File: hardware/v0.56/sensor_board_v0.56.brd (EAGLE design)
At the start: 50.8 x 50.8 mm, 63 parts, among them J3 USB-MICROB, U10 TSL2591, U11 915MHz, U3 OPA344, U4 SI7021, U5 ATMEGA328P-MU, U6 ADMP401, U7 PMS7003, U8 MCP1703CB, U9 BMP280, X1 16 MHz

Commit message: update
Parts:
- added R9: 100K, Adafruit Feather 32u4 Bluefruit LE:MICROBUILDER__0402MP
- moved U$7 0.28 mm to (35.2, 1.42)
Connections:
- new net A1: U5.24
- new net A2: U5.25
- new net A3: U5.26
- new net A6: U5.19
- new net A7: U5.22
- new net N$13: R9.2, U$7.1
- net D5: now also U$7.7
- net GND: now also C2.1, J2.1, U$7.11
- net PWR: now also J2.2
- net SCL: now also U$7.10
- net SDA: now also U$7.9
- net VCC: now also C2.2, R9.1, U$7.6

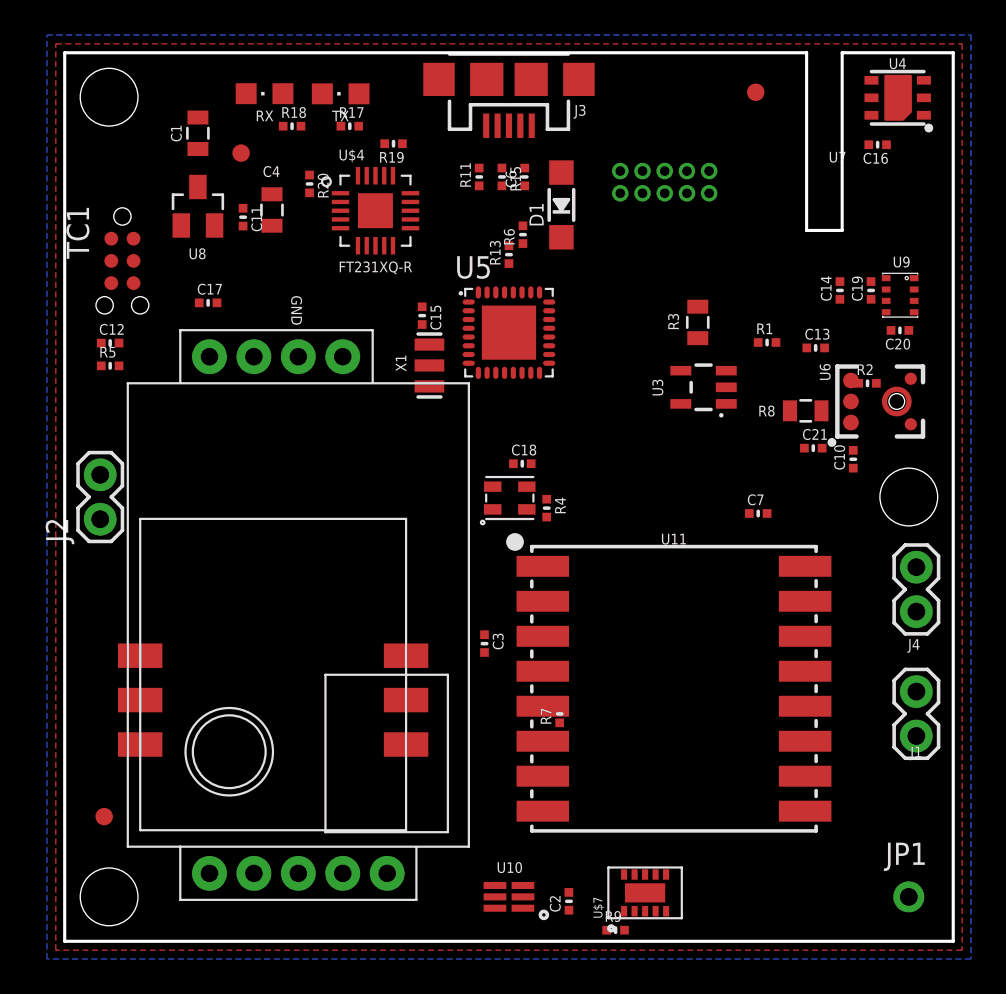
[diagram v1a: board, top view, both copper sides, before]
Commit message: Added Power Booster circuit; a lot of rearrangments
circuit traces still incomplete
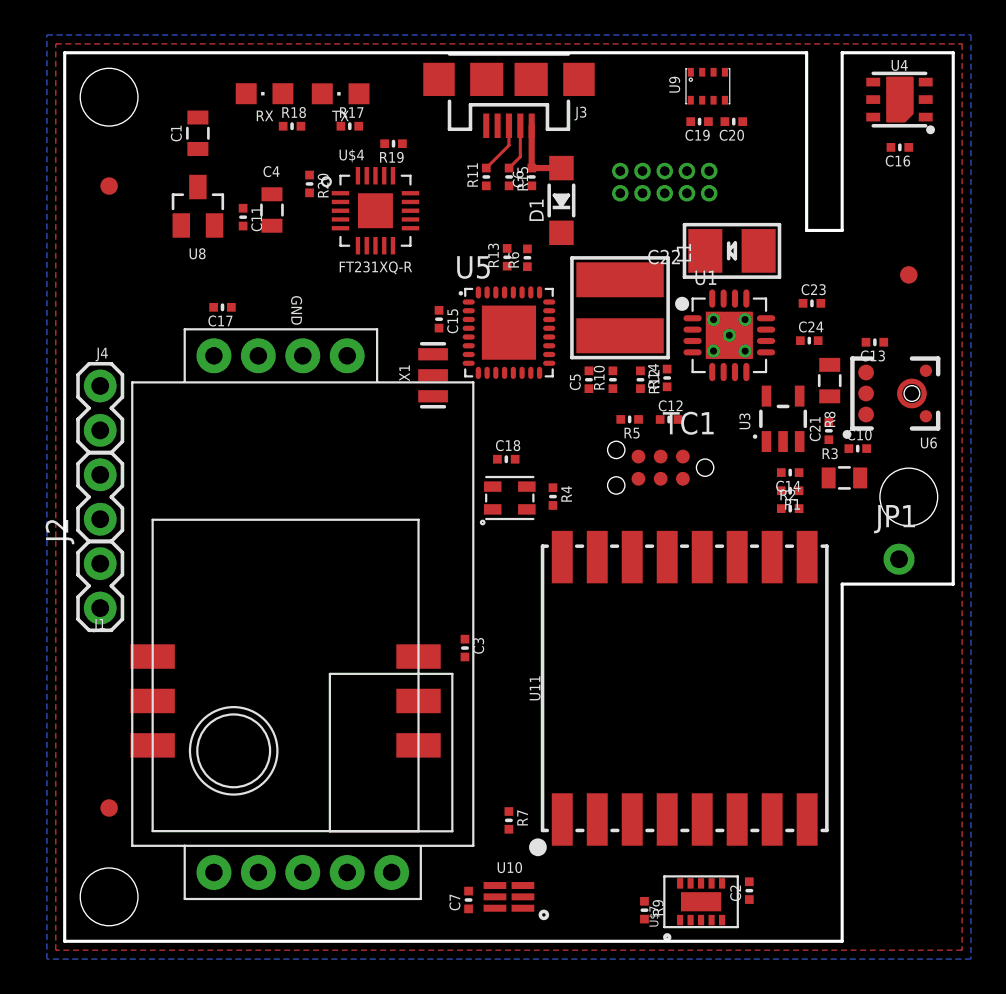
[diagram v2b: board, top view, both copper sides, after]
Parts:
- added C22: 100uF/6V, microbuilder:EIA3528-21/B-R
- added C23: 0.1uF, Adafruit Feather 32u4 Bluefruit LE:MICROBUILDER__0402MP
- added C24: 10uF, Adafruit Feather 32u4 Bluefruit LE:MICROBUILDER__0402MP
- added C5: 2.2uF, Adafruit Feather 32u4 Bluefruit LE:MICROBUILDER__0402MP
- added L1: VLC5045-6.8uH, microbuilder:INDUCTOR_5X5MM_TDK_VLC5045
- added R10: 1.87M, Adafruit Feather 32u4 Bluefruit LE:MICROBUILDER__0402MP
- added R12: 200K, Adafruit Feather 32u4 Bluefruit LE:MICROBUILDER__0402MP
- added R14: 340K, Adafruit Feather 32u4 Bluefruit LE:MICROBUILDER__0402MP
- added U1: TPS61090RSAR, microbuilder:PVQFN-16
- moved J4 47.3 mm to (2.03, 29.2), turned to 90 degrees
- moved J1 47.2 mm to (2.03, 19.1)
- moved TC1 33.0 mm to (34.1, 27.1), turned to 180 degrees
- moved C12 32.3 mm to (34.6, 29.8)
- moved R5 29.9 mm to (32.3, 29.8), turned to 180 degrees
- moved C7 27.6 mm to (23.1, 2.36), turned to 90 degrees
- moved JP1 19.3 mm to (47.7, 21.8)
- moved U9 16.2 mm to (36.8, 48.9), turned to 180 degrees
- moved C20 15.3 mm to (38.3, 46.9)
- moved C19 13.8 mm to (36.3, 46.9), turned to 180 degrees
- moved U$3 13.6 mm to (48.3, 38.1)
- moved R3 12.2 mm to (44.6, 26.5), turned to 0 degrees
- moved C14 10.8 mm to (41.5, 26.8), turned to 180 degrees
- moved C2 10.3 mm to (39.1, 2.90)
- moved R1 8.58 mm to (41.5, 25.8), turned to 180 degrees
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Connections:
- new net 5.0V: C22.+, C5.2, R10.2, U1.1, U1.15, U1.16
- new net ENABLE: R14.1, U1.11
- new net N$12: R10.1, R12.2, U1.14
- new net N$6: L1.P$2, U1.3, U1.4
- new net VBAT: R14.2
- net GND: now also C22.-, C23.1, C24.1, C5.1, R12.1, U1.10, U1.13, U1.5, U1.6, U1.7, U1.P$18, U1.P$19, U1.P$20, U1.P$21, U1.P$22, U1.THERMAL
- net PWR: now also C23.2, C24.2, L1.P$1, U1.8
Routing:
- net VBUS: track 0.00 -> 4.12 mm
- net N$33: track 0.00 -> 2.95 mm
- net N$32: track 0.00 -> 2.68 mm
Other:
- outline, holes or cut-outs redrawn
- board text removed: "U7"

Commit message: Adjustments
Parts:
- removed J4: (no value), SparkFun-Connectors:1X02
- moved C23 35.9 mm to (6.81, 37.7), turned to 90 degrees
- moved C24 34.2 mm to (8.59, 37.7), turned to 90 degrees
- moved RX 31.3 mm to (39.9, 35.4), turned to 0 degrees
- moved R18 27.9 mm to (38.1, 34.4), turned to 180 degrees
- moved TX 25.7 mm to (39.9, 39.4), turned to 0 degrees
- moved C22 25.3 mm to (14.1, 47.4), turned to 0 degrees
- moved U1 25.0 mm to (13.9, 41.5), turned to 270 degrees
- moved L1 24.8 mm to (7.62, 42.1), turned to 90 degrees
- moved R17 23.3 mm to (38.1, 38.2)
- moved R20 23.0 mm to (36.0, 36.6)
- moved J1 21.6 mm to (2.03, 40.6)
- moved C5 20.3 mm to (14.4, 45.1), turned to 0 degrees
- moved R14 18.2 mm to (17.4, 38.6), turned to 270 degrees
- moved R12 17.7 mm to (17.4, 40.6), turned to 90 degrees
- moved R19 17.5 mm to (31.6, 33.6), turned to 0 degrees
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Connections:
- removed net 5.0V: C22.+, C5.2, R10.2, U1.1, U1.15, U1.16
- new net 5V: C17.2, C22.+, C5.2, R10.2, U$6.VIN, U1.1, U1.15, U1.16
- net GND: now also U1.9; no longer J4.1
- net PWR: no longer C17.2, U$6.VIN
- net VCC: no longer J4.2

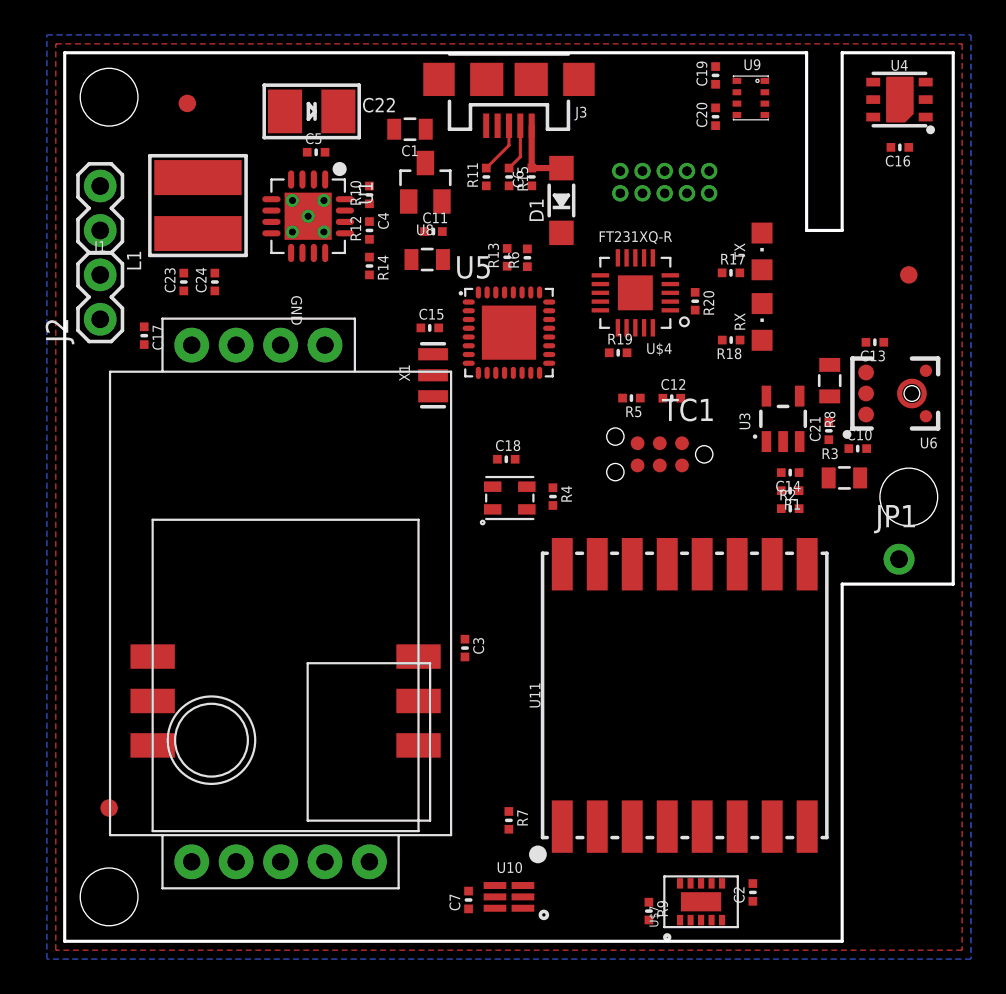
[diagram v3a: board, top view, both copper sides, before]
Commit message: Added notches in the board
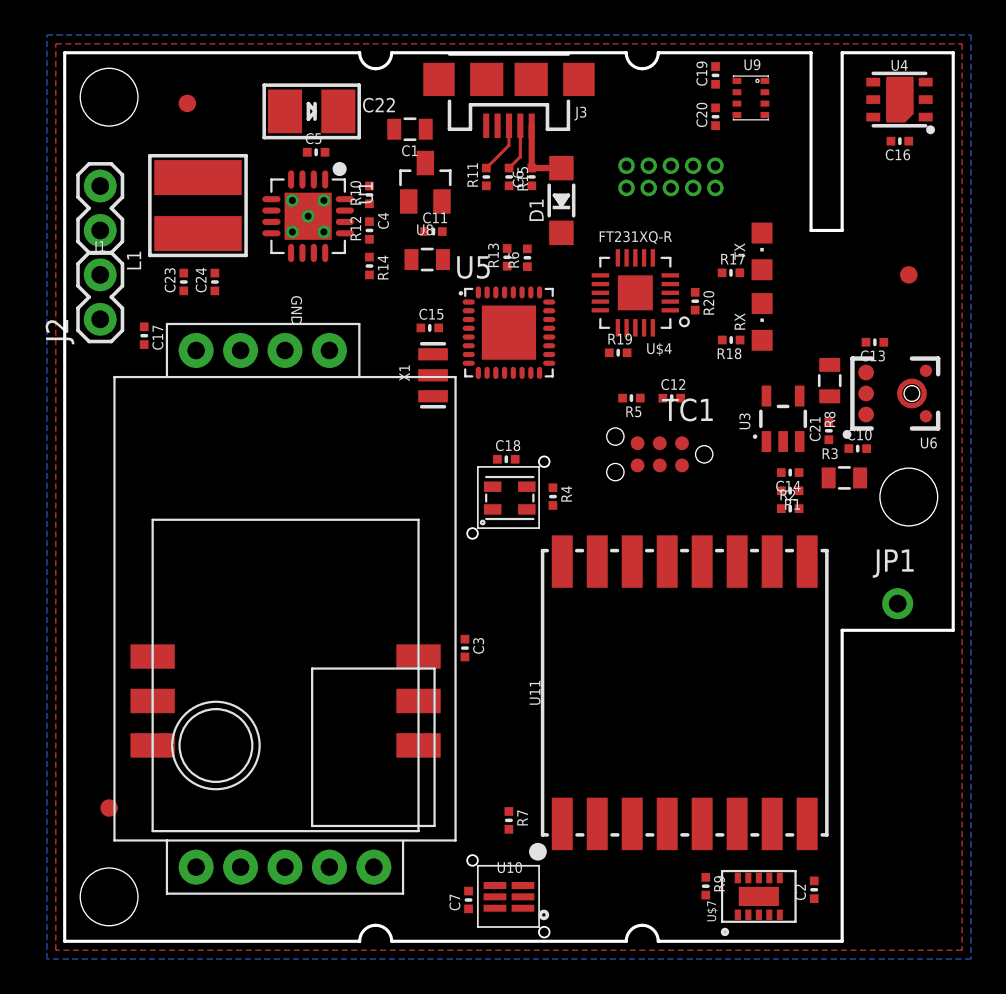
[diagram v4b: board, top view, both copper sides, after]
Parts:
- added U$12, U$9: VLP-450-F, VLP-450-F:VLP-450-F
- moved R9 3.55 mm to (36.7, 3.15)
- moved C2 3.51 mm to (42.8, 2.95)
- moved U$7 3.32 mm to (41.7, 1.22)
- moved JP1 2.54 mm to (47.6, 19.3)
- moved U7 0.47 mm to (42.1, 49.2)
- moved U$6 0.40 mm to (2.85, 35.3)
- moved C16 0.36 mm to (47.7, 45.7)
- moved U11 0.15 mm to (35.4, 14.2)
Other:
- outline, holes or cut-outs redrawn

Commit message: v0.56 - completed
DRC & ERC checked
Features:
- Board dimensions and component placement completely redesigned
- Neopixel Mini replaced by NeoPixel Nano 2427
- Light pipes for NeoPixel and Light sensor
- SHT31 replaced with Si7021
- Added three mounting holes
- Cutout for the helical antenna
- CCS811 VOC sensor added
- MH-z19 CO2 sensor pads added (can be replaced with IAQ core - pads
also available) (can also be replaced by S8 CO2 sensor in future for
larger orders)
- ATMEGA328P-AU replaced by ATMEGA328P-MU (QFN)
- FT232RL replaced by FT231XQ (QFN)
- Notches in PCB for attaching to enclosure
- 0805 Diode replaced with SOD123
- ISP headers replaced with TagConnect
- Better thermal isolation for T/RH sensor
- I2C & power headers moved to left
- Several 0805 components replaced by 0402 ones
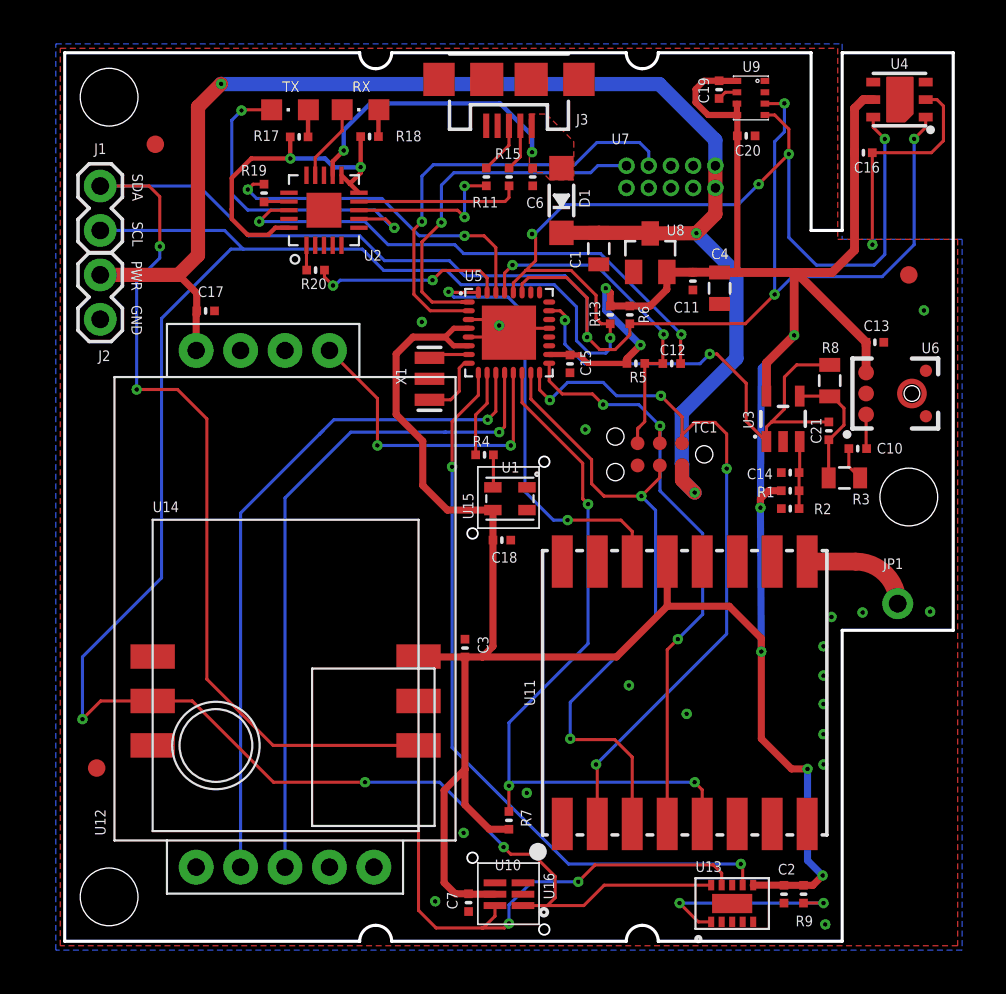
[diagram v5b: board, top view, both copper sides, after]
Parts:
- removed C22: 100uF/6V, microbuilder:EIA3528-21/B-R
- removed C23: 0.1uF, Adafruit Feather 32u4 Bluefruit LE:MICROBUILDER__0402MP
- removed C24: 10uF, Adafruit Feather 32u4 Bluefruit LE:MICROBUILDER__0402MP
- removed C5: 2.2uF, Adafruit Feather 32u4 Bluefruit LE:MICROBUILDER__0402MP
- removed L1: VLC5045-6.8uH, microbuilder:INDUCTOR_5X5MM_TDK_VLC5045
- removed R10: 1.87M, Adafruit Feather 32u4 Bluefruit LE:MICROBUILDER__0402MP
- removed R12: 200K, Adafruit Feather 32u4 Bluefruit LE:MICROBUILDER__0402MP
- removed R14: 340K, Adafruit Feather 32u4 Bluefruit LE:MICROBUILDER__0402MP
- removed U$12: VLP-450-F, VLP-450-F:VLP-450-F
- removed U$4: FT231XQ-R, ftdi_ft231xq-r:FTDI_FT231XQ-R_PACKAGE
- removed U$5: NEOPIXEL_NANO_2427, NeoPixel Nano 2427:SK6805-2427
- removed U$7: CCS811-I2C, CCS811:LGA
- added U13: CCS811-I2C, CCS811:LGA
- added U16: VLP-450-F, VLP-450-F:VLP-450-F
- added U2: FT231XQ-R, ftdi_ft231xq-r:FTDI_FT231XQ-R_PACKAGE
- D1: value (none) -> SOD123
- U1: value TPS61090RSAR -> NEOPIXEL_NANO_2427; device microbuilder:PVQFN-16 -> NeoPixel Nano 2427:SK6805-2427
- U7: device Amphenol:RECEPTACLE_1.27MM_2X5 -> Amphenol:PMS7003_RECEPTACLE_1.27MM_2X5
- moved TX 28.2 mm to (12.9, 47.5), turned to 90 degrees
- moved RX 26.0 mm to (16.9, 47.5), turned to 90 degrees
- moved R17 25.9 mm to (13.4, 46.0)
- moved R18 23.7 mm to (17.4, 46.0)
- moved R19 22.2 mm to (11.4, 42.8), turned to 270 degrees
- moved R20 21.8 mm to (14.3, 38.4), turned to 180 degrees
- moved U1 20.1 mm to (24.1, 24.1), turned to 0 degrees
- moved C4 16.8 mm to (37.4, 37.3), turned to 270 degrees
- moved C11 15.1 mm to (35.9, 37.7), turned to 90 degrees
- moved U8 13.5 mm to (33.5, 39.4)
- moved C1 12.8 mm to (30.5, 39.6), turned to 270 degrees
- moved C15 8.28 mm to (28.9, 33.0), turned to 90 degrees
- moved R13 6.75 mm to (31.2, 35.8)
- moved R6 6.70 mm to (32.3, 35.8)
- moved R9 5.61 mm to (42.2, 2.69)
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- renumbered U$6 to U12, U$8 to U14, U$9 to U15
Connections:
- removed net 5V: C17.2, C22.+, C5.2, R10.2, U1.1, U1.15, U1.16, U12.VIN
- removed net ENABLE: R14.1, U1.11
- removed net N$12: R10.1, R12.2, U1.14
- removed net N$6: L1.P$2, U1.3, U1.4
- removed net VBAT: R14.2
- net D3: now also U7.9; no longer U7.7
- net D4: now also U7.7; no longer U7.9
- net D5: now also U13.7; no longer U$7.7
- net DTR: now also U2.DTR#; no longer U$4.DTR#
- net FTDI_VCC: now also U2.3V3OUT, U2.RESET#, U2.VCCIO; no longer U$4.3V3OUT, U$4.RESET#, U$4.VCCIO
- net GND: now also U1.GND, U13.11, U2.GND_PIN13, U2.GND_PIN21, U2.GND_PIN3; no longer C22.-, C23.1, C24.1, C5.1, R12.1, U$4.GND_PIN13, U$4.GND_PIN21, U$4.GND_PIN3, U$5.GND, U$7.11, U1.10, U1.13, U1.5, U1.6, U1.7, U1.9, U1.P$18, U1.P$19, U1.P$20, U1.P$21, U1.P$22, U1.THERMAL
- net N$1: now also U1.DIN; no longer U$5.DIN
- net N$13: now also U13.1; no longer U$7.1
- net N$17: now also U2.CBUS1; no longer U$4.CBUS1
- net N$18: now also U2.CBUS2; no longer U$4.CBUS2
- net N$2: now also U2.RXD; no longer U$4.RXD
- net N$25: now also U2.USBDM; no longer U$4.USBDM
- net N$26: now also U2.USBDP; no longer U$4.USBDP
- net N$3: now also U2.TXD; no longer U$4.TXD
- net PWR: now also C17.2, U12.VIN; no longer C23.2, C24.2, L1.P$1, U1.8
- net SCL: now also U13.10; no longer U$7.10
- net SDA: now also U13.9; no longer U$7.9
- net VBUS: now also U2.VCC; no longer U$4.VCC
- net VCC: now also U1.VCC, U13.6; no longer U$5.VCC, U$7.6
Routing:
- net VCC: track 0.00 -> 181.4 mm, vias 0 -> 7
- net SDA: track 0.00 -> 161.7 mm, vias 0 -> 8
- net SCL: track 0.00 -> 160.4 mm, vias 0 -> 8
- net PWR: track 0.00 -> 83.5 mm, vias 0 -> 3
- net D5: track 0.00 -> 42.6 mm, vias 0 -> 2
- net SS: track 0.00 -> 41.8 mm, vias 0 -> 3
- net MISO: track 0.00 -> 41.1 mm, vias 0 -> 4
- net D7: track 0.00 -> 39.8 mm, vias 0 -> 1
- net D8: track 0.00 -> 38.5 mm, vias 0 -> 1
- net MOSI: track 0.00 -> 37.1 mm, vias 0 -> 2
- net SCK: track 0.00 -> 34.0 mm, vias 0 -> 3
- net DTR: track 0.00 -> 30.5 mm, vias 0 -> 2
- net A0: track 0.00 -> 28.5 mm, vias 0 -> 2
- net D2: track 0.00 -> 25.6 mm, vias 0 -> 2
- net D4: track 0.00 -> 25.3 mm, vias 0 -> 1
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- added copper zone on layer 1, net VBUS
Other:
- board text added: "PWR"
- board text added: "SCL"
- board text added: "SDA"
